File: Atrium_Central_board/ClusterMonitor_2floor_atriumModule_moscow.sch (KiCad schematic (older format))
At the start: 36 parts, among them J1 RJ32_Shielded, J2 Conn_01x07, SW1 SW_SPST, SW2 ADDRESS_SELECT, SW3 SW_SPDT, U1 AMS1117-3.3, U2 STM32F030C8Tx

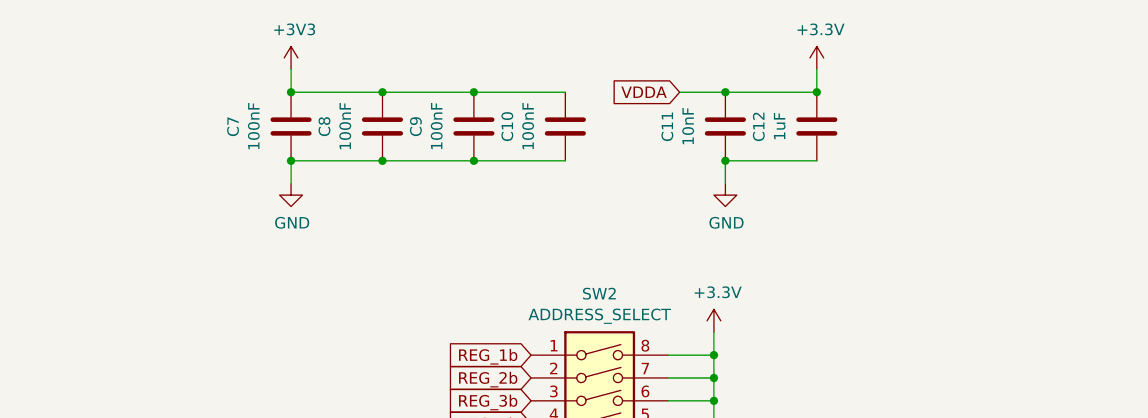
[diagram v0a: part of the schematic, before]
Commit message: Some changes
Add stencil board layout.
Add gerbers.
Minor changes in expancion and atrium board.
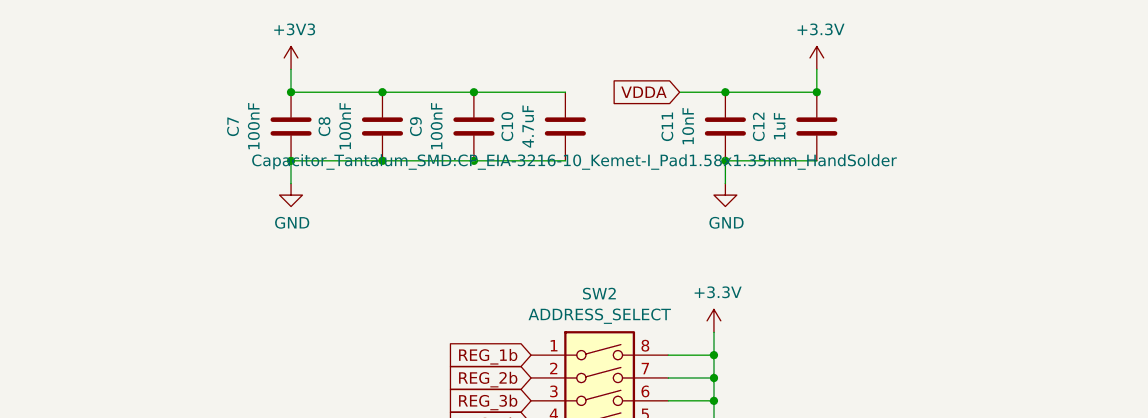
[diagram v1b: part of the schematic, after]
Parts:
- C10: value 100nF -> 4.7uF; footprint Capacitor_SMD:C_0402_1005Metric_Pad0.74x0.62mm_HandSolder -> Capacitor_Tantalum_SMD:CP_EIA-3216-10_Kemet-I_Pad1.58x1.35mm_HandSolder
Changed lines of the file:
@@
 P 9800 1050
 F 0 "C10" V 9548 1050 50  0000 C CNN
-F 1 "100nF" V 9639 1050 50  0000 C CNN
-F 2 "Capacitor_SMD:C_0402_1005Metric_Pad0.74x0.62mm_HandSolder" H 9838 900 50  0001 C CNN
+F 1 "4.7uF" V 9639 1050 50  0000 C CNN
+F 2 "Capacitor_Tantalum_SMD:CP_EIA-3216-10_Kemet-I_Pad1.58x1.35mm_HandSolder" H 9838 900 50  0000 C CNN
 F 3 "~" H 9800 1050 50  0001 C CNN
 	1    9800 1050
